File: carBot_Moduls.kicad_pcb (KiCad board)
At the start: 2 copper layers, 5 parts, among them J12 Conn_01x06

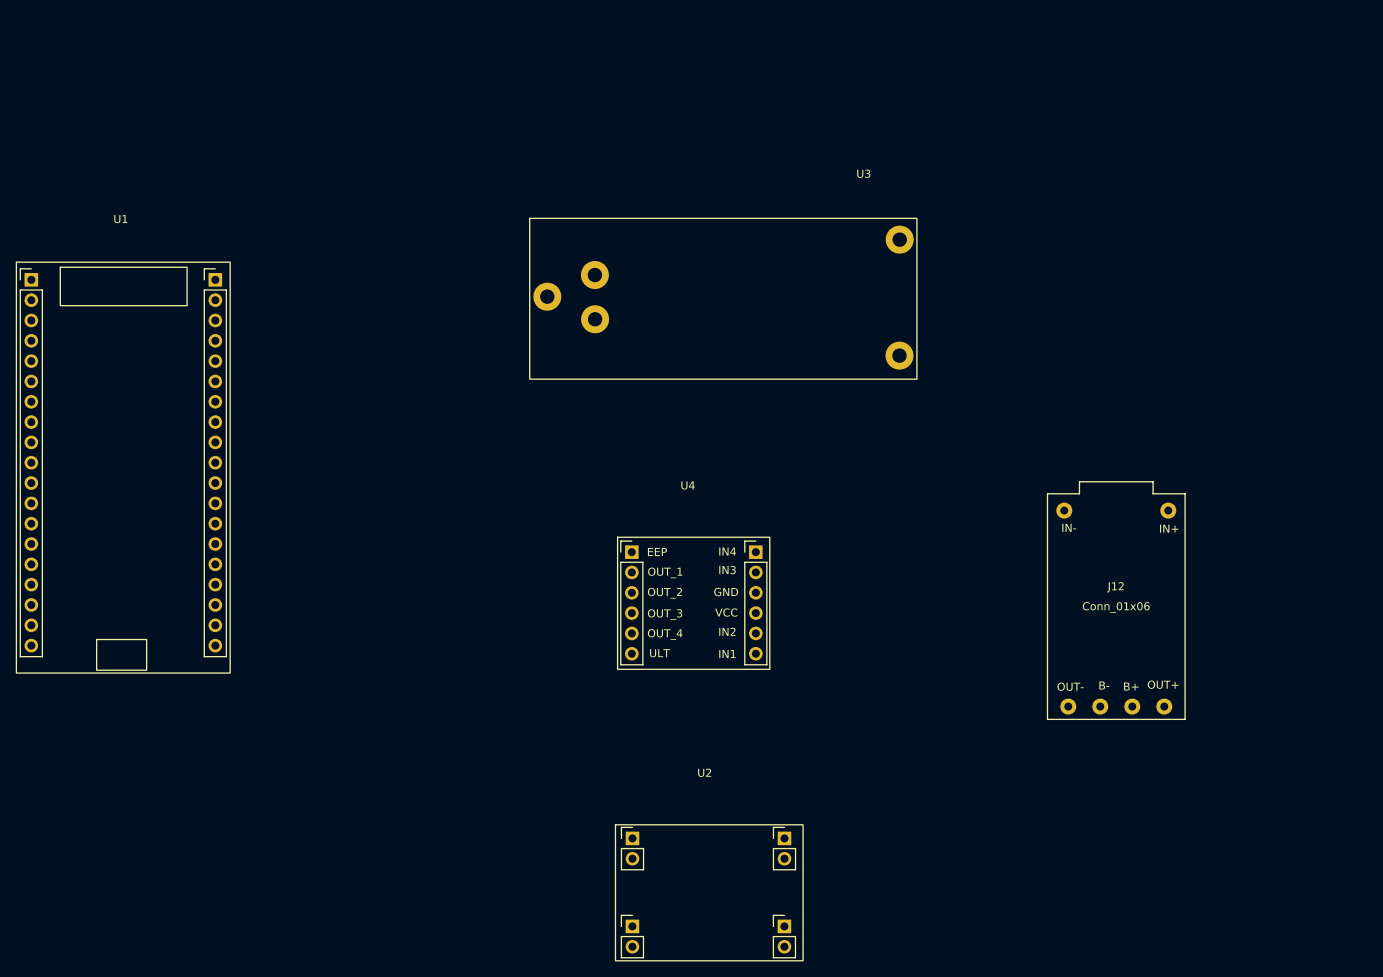
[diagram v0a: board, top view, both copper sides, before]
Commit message: assgin footprint
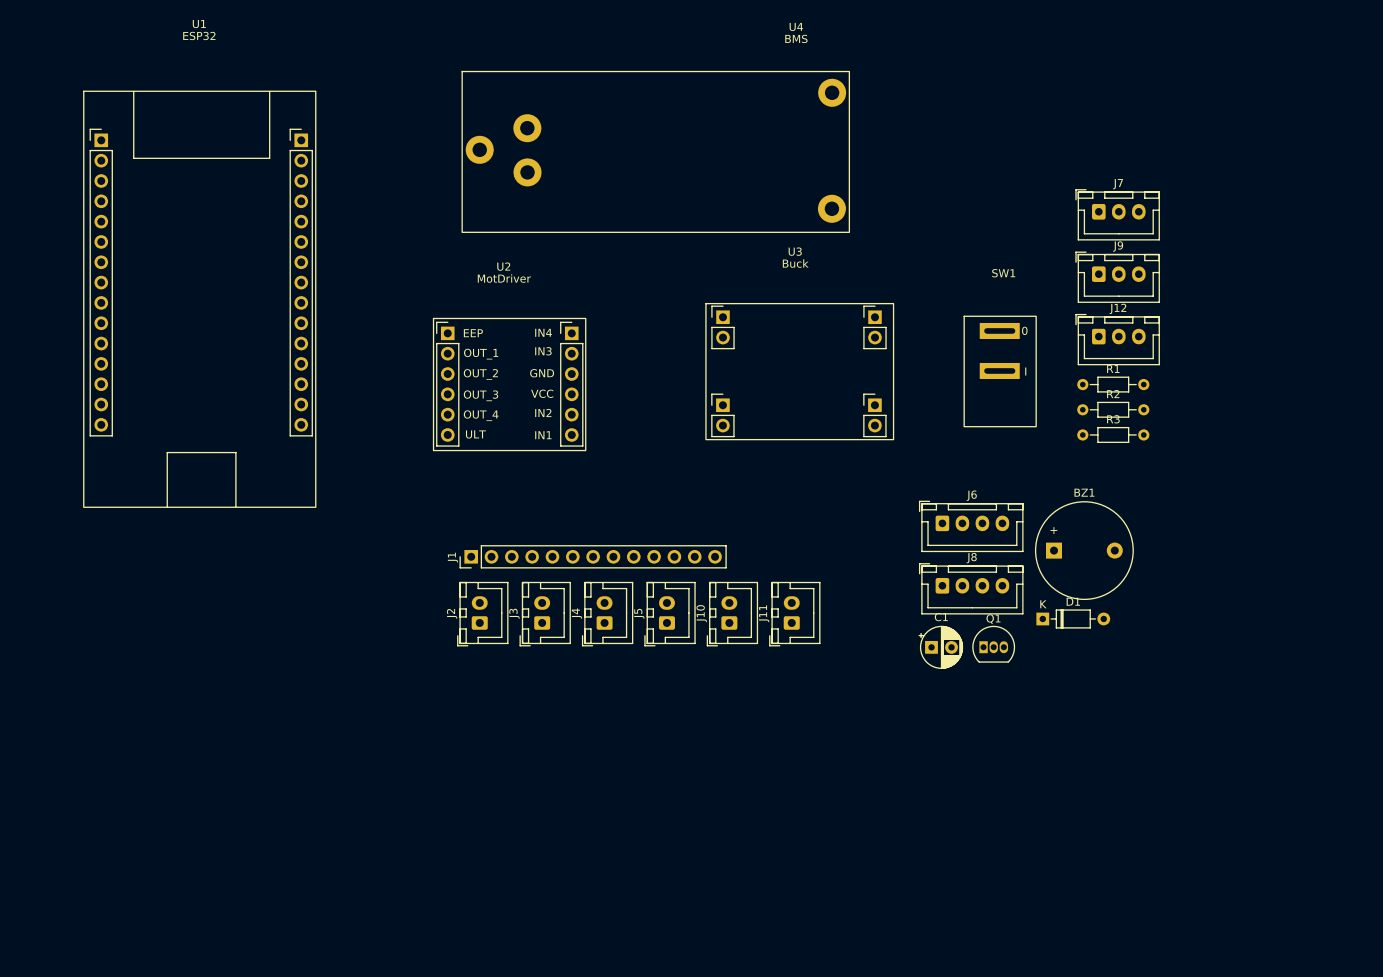
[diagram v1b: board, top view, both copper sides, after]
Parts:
- added BZ1: Buzzer, Buzzer_Beeper:Buzzer_12x9.5RM7.6, F.Cu at (180.8, 88.5)
- added C1: 470uF, Capacitor_THT:CP_Radial_D5.0mm_P2.50mm, F.Cu at (165.5, 100.5)
- added D1: 1N4148, Diode_THT:D_DO-35_SOD27_P7.62mm_Horizontal, F.Cu at (179.4, 97.0)
- added J1: ESP_PIN, Connector_PinHeader_2.54mm:PinHeader_1x13_P2.54mm_Vertical, F.Cu at (107.9, 89.2)
- added J10: Batt_1, Connector_JST:JST_XH_B2B-XH-A_1x02_P2.50mm_Vertical, F.Cu at (140.2, 97.5)
- added J11: Batt_2, Connector_JST:JST_XH_B2B-XH-A_1x02_P2.50mm_Vertical, F.Cu at (148.0, 97.5)
- added J2: Conn_MOT_FL, Connector_JST:JST_XH_B2B-XH-A_1x02_P2.50mm_Vertical, F.Cu at (109.0, 97.5)
- added J3: Conn_MOT_RL, Connector_JST:JST_XH_B2B-XH-A_1x02_P2.50mm_Vertical, F.Cu at (116.8, 97.5)
- added J4: Conn_MOT_FR, Connector_JST:JST_XH_B2B-XH-A_1x02_P2.50mm_Vertical, F.Cu at (124.6, 97.5)
- added J5: Conn_MOT_RR, Connector_JST:JST_XH_B2B-XH-A_1x02_P2.50mm_Vertical, F.Cu at (132.4, 97.5)
- added J6: UltraSonic, Connector_JST:JST_XH_B4B-XH-A_1x04_P2.50mm_Vertical, F.Cu at (166.8, 85.0)
- added J7: RGB_LED_F, Connector_JST:JST_XH_B3B-XH-A_1x03_P2.50mm_Vertical, F.Cu at (186.4, 46.1)
- added J8: OLED, Connector_JST:JST_XH_B4B-XH-A_1x04_P2.50mm_Vertical, F.Cu at (166.8, 92.8)
- added J9: IR_sensor, Connector_JST:JST_XH_B3B-XH-A_1x03_P2.50mm_Vertical, F.Cu at (186.4, 53.9)
- added Q1: BC547, Package_TO_SOT_THT:TO-92_Inline, F.Cu at (172.0, 100.5)
- added R1: 1K, Resistor_THT:R_Axial_DIN0204_L3.6mm_D1.6mm_P7.62mm_Horizontal, F.Cu at (184.4, 67.7)
- added R2: 330, Resistor_THT:R_Axial_DIN0204_L3.6mm_D1.6mm_P7.62mm_Horizontal, F.Cu at (184.4, 70.8)
- added R3: 330, Resistor_THT:R_Axial_DIN0204_L3.6mm_D1.6mm_P7.62mm_Horizontal, F.Cu at (184.4, 74.0)
- added SW1: SW_SPST, CarBotLibrary:KCD1-11_ON_OFF, F.Cu at (174.5, 54.3)
- J12: value Conn_01x06 -> RGB_LED_B; footprint CarBotLibrary:TP4056_TypeC_Module -> Connector_JST:JST_XH_B3B-XH-A_1x03_P2.50mm_Vertical
- U1: value ~ -> ESP32; footprint CarBotLibrary:ESP32-38pins -> CarBotLibrary:ESP32-30pins
- U2: value ~ -> MotDriver; footprint CarBotLibrary:Buck -> CarBotLibrary:MotDriver
- U3: value ~ -> Buck; footprint CarBotLibrary:BMS -> CarBotLibrary:Buck
- U4: value ~ -> BMS; footprint CarBotLibrary:MotDriver -> CarBotLibrary:BMS
- moved U2 68.1 mm to (112.0, 53.5)
- moved U4 58.9 mm to (148.6, 23.5)
- moved J12 33.8 mm to (186.4, 61.7)
- moved U1 26.3 mm to (73.9, 23.2)
- moved U3 13.0 mm to (148.4, 51.6)
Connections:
- J12 pad 1: unconnected-(J12-Pin_1-Pad1) -> Net-(J12-Pin_1)
- J12 pad 2: unconnected-(J12-Pin_2-Pad2) -> /+5V
- J12 pad 3: unconnected-(J12-Pin_3-Pad3) -> /GND
- U1 pad 1: /3.3V -> unconnected-(U1-EN-Pad1)
- U1 pad 10: /M_IN2 -> /SONAR_TRIG
- U1 pad 11: /M_IN3 -> /IR_DATA
- U1 pad 12: /M_IN4 -> unconnected-(U1-D12-Pad12)
- U1 pad 13: /SONAR_ECHO -> /LED_DATA_B
- U1 pad 15: /SONAR_TRIG -> /+5V
- U1 pad 16: unconnected-(U1-Pin_16-Pad16) -> /3.3V
- U1 pad 17: unconnected-(U1-Pin_17-Pad17) -> /GND
- U1 pad 18: unconnected-(U1-Pin_18-Pad18) -> /LED_DATA_F
- U1 pad 19: /+5V -> /D2
- U1 pad 20: unconnected-(U1-Pin_20-Pad20) -> /D4
- U1 pad 21: unconnected-(U1-Pin_21-Pad21) -> /RX2
- U1 pad 22: unconnected-(U1-Pin_22-Pad22) -> /TX2
- U1 pad 23: /LED_DATA_F -> /D5
- U1 pad 24: unconnected-(U1-Pin_24-Pad24) -> /D18
- U1 pad 25: unconnected-(U1-Pin_25-Pad25) -> /D19
- U1 pad 26: unconnected-(U1-Pin_26-Pad26) -> /OLED_SDA
- U1 pad 29: unconnected-(U1-Pin_29-Pad29) -> /OLED_SCL
- U1 pad 30: unconnected-(U1-Pin_30-Pad30) -> /Buzzer_EN
- U1 pad 4: unconnected-(U1-Pin_4-Pad4) -> /SONAR_ECHO
- U1 pad 5: unconnected-(U1-Pin_5-Pad5) -> /ULT
- U1 pad 6: unconnected-(U1-Pin_6-Pad6) -> /M_IN1
- U1 pad 7: /LED_DATA_B -> /M_IN2
- U1 pad 8: unconnected-(U1-Pin_8-Pad8) -> /M_IN3
- U1 pad 9: /M_IN1 -> /M_IN4

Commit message: Routing and generate Gerber
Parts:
- added D2: Power_ON, LED_THT:LED_D3.0mm, F.Cu at (173.5, 59.8)
- added D3: LED (Blue, Green), LED_THT:LED_D3.0mm, F.Cu at (94.2, 54.6)
- added H1: ~, MountingHole:MountingHole_3mm, F.Cu at (112.3, 108.0)
- added H2: ~, MountingHole:MountingHole_3mm, F.Cu at (184.3, 107.8)
- added H3: ~, MountingHole:MountingHole_3mm, F.Cu at (184.4, 53.8)
- added R4: 1K, Resistor_THT:R_Axial_DIN0204_L3.6mm_D1.6mm_P7.62mm_Horizontal, F.Cu at (168.5, 55.9)
- added R5: 10K, Resistor_THT:R_Axial_DIN0204_L3.6mm_D1.6mm_P7.62mm_Horizontal, F.Cu at (94.6, 108.7)
- added R6: 330, Resistor_THT:R_Axial_DIN0204_L3.6mm_D1.6mm_P7.62mm_Horizontal, F.Cu at (81.6, 55.0)
- added SW2: B1, Button_Switch_THT:SW_PUSH_6mm, F.Cu at (85.2, 104.3)
- J2: value Conn_MOT_FL -> Conn_MOT_FR
- J3: value Conn_MOT_RL -> Conn_MOT_RR
- J4: value Conn_MOT_FR -> Conn_MOT_FL
- J5: value Conn_MOT_RR -> Conn_MOT_RL
- moved J7 105.9 mm to (83.0, 69.5), turned to 90 degrees
- moved U1 96.2 mm to (111.7, 111.6), turned to 180 degrees
- moved R2 95.4 mm to (89.7, 59.1), turned to 180 degrees
- moved J6 84.7 mm to (83.3, 99.3), turned to 90 degrees
- moved J8 83.8 mm to (83.5, 84.0), turned to 90 degrees
- moved J10 80.3 mm to (214.1, 66.1), turned to -90 degrees
- moved J11 78.8 mm to (214.4, 55.2), turned to -90 degrees
- moved U4 60.7 mm to (198.3, 58.3)
- moved J3 51.5 mm to (151.5, 59.4), turned to 180 degrees
- moved J2 48.2 mm to (139.0, 59.7), turned to 180 degrees
- moved U3 48.1 mm to (188.3, 78.5)
- moved J9 47.8 mm to (213.7, 93.1), turned to -90 degrees
- moved U2 47.0 mm to (153.1, 76.3), turned to -90 degrees
- moved R1 39.7 mm to (160.6, 99.4)
- moved J12 33.2 mm to (213.9, 80.3), turned to -90 degrees
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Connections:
- J1 pad 10: unconnected-(J1-Pin_10-Pad10) -> /GND
- J1 pad 11: /GND -> /+5V
- J1 pad 12: /3.3V -> /GND
- J1 pad 13: /+5V -> /3.3V
- U1 pad 10: /SONAR_TRIG -> /SONAR_ECHO
- U1 pad 11: /IR_DATA -> /SONAR_TRIG
- U1 pad 12: unconnected-(U1-D12-Pad12) -> /user_led
- U1 pad 28: unconnected-(U1-TX0-Pad28) -> /user_button
- U1 pad 30: /Buzzer_EN -> unconnected-(U1-D23-Pad30)
- U1 pad 4: /SONAR_ECHO -> /IR_DATA
- U1 pad 5: /ULT -> /Buzzer_EN
- U2 pad 6: /ULT -> unconnected-(U2-Pin_6-Pad6)
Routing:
- net /+5V: track 0.00 -> 342.3 mm, vias 0 -> 2
- net /3.3V: track 0.00 -> 288.6 mm, vias 0 -> 3
- net /LED_DATA_B: track 0.00 -> 180.4 mm
- net /IR_DATA: track 0.00 -> 113.7 mm
- net /BM_4.2V: track 0.00 -> 92.9 mm
- net /SONAR_ECHO: track 0.00 -> 90.3 mm
- net /SONAR_TRIG: track 0.00 -> 86.5 mm
- net /OUT_4: track 0.00 -> 68.0 mm
- net /OUT_3: track 0.00 -> 64.3 mm
- net /Buzzer_EN: track 0.00 -> 61.7 mm
- net /user_led: track 0.00 -> 38.9 mm
- net /8.4V: track 0.00 -> 38.5 mm
- net /user_button: track 0.00 -> 35.4 mm
- net /LED_DATA_F: track 0.00 -> 34.5 mm
- net Net-(SW1-B): track 0.00 -> 33.0 mm
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- added copper zone on B.Cu, net /GND
- added copper zone on F.Cu, net /GND
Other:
- board outline added: 143 x 65 mm
- board text added: "+"
- board text added: "-"
- board text added: "3.3V"
- board text added: "5V"
- board text added: "D18"
- board text added: "D19"
- board text added: "D2"
- board text added: "D4"
- board text added: "D5"
- board text added: "DIN"
- board text added: "ECHO"
- board text added: "GND"
- board text added: "IR_D"
- board text added: "RX2"
- board text added: "SCL"
- board text added: "SDA"
- board text added: "TRIG"
- board text added: "TX2"

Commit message: Add Logo To PCB
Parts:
- added G***: LOGO, CarBotLibrary:BotLogo_Big, F.Cu at (211.0, 107.8)
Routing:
- net /3.3V: track 288.6 -> 291.3 mm
- net /GND: vias 45 -> 46

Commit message: Add carbot modules-v2
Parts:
- removed the G*** at (211.0, 107.8)
- added G***: LOGO, CarBotLibrary:EZ-BotixLogo, F.Cu at (208.7, 106.8)
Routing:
- net /3.3V: track 291.3 -> 288.6 mm
